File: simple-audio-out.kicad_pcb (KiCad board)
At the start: 2 copper layers, 49.5 x 72.4 mm, 12 parts, among them J1 Conn_01x04, Q1 2N3904

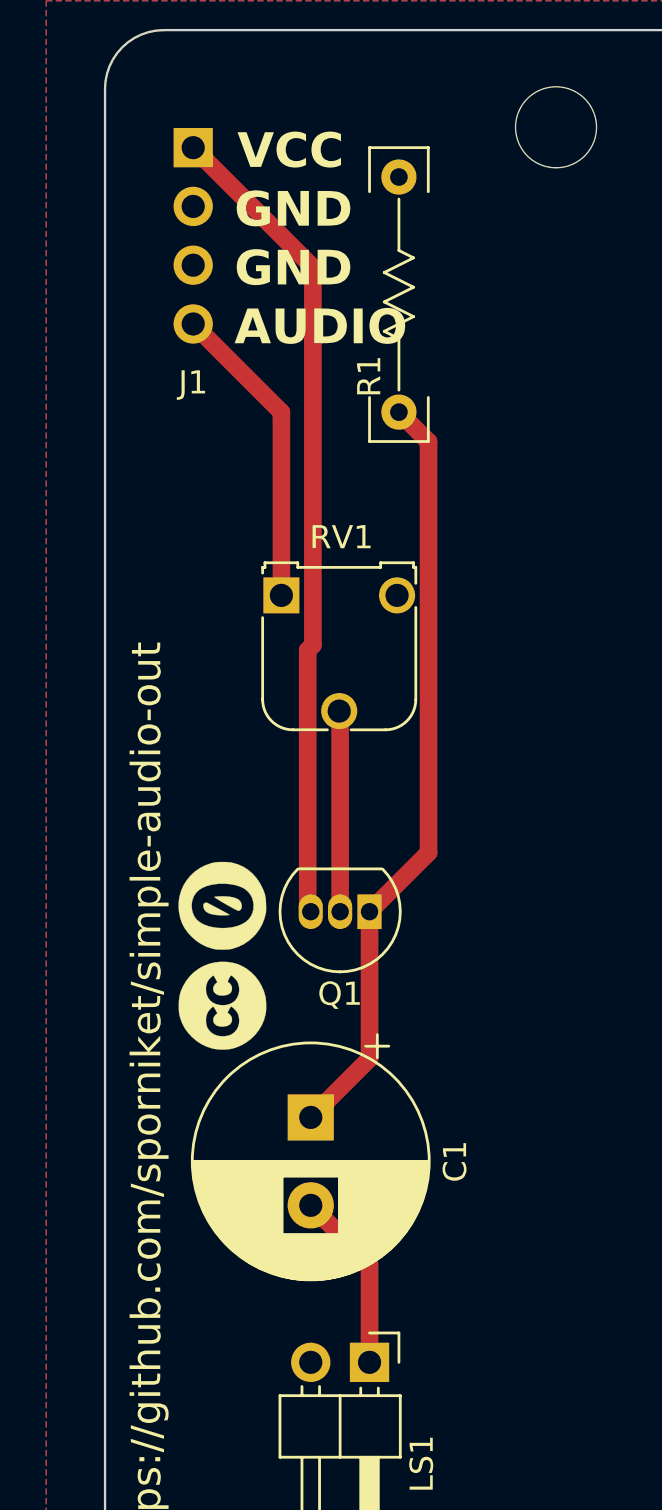
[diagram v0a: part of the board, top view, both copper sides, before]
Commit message: #1 -- change the footprint of Q1 for easier assembly
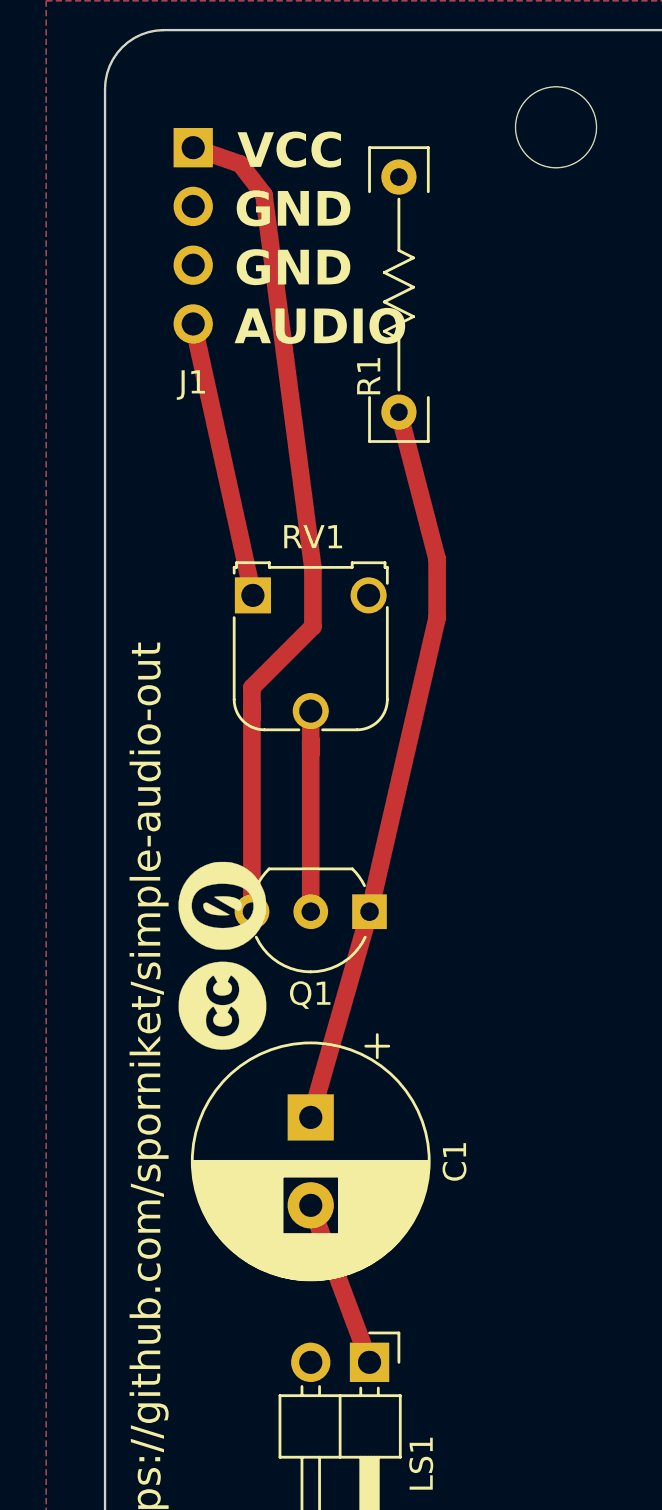
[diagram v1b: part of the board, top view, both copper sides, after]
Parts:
- Q1: footprint Package_TO_SOT_THT:TO-92_Inline -> Package_TO_SOT_THT:TO-92_Inline_Wide
- moved RV1 1.23 mm to (118.2, 43.5)
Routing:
- net Net-(Q1-E): track 33.1 -> 31.4 mm
- net /AUDIO_IN: track 13.3 -> 12.0 mm
- net /VCC: track 35.3 -> 36.5 mm
- net Net-(Q1-B): track 8.69 -> 9.44 mm
- net Net-(C1-Pad2): track 7.84 -> 7.24 mm
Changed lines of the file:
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@@
   (net 5 "/AUDIO_IN")
   (net 6 "Net-(Q1-B)")
-  (footprint "Package_TO_SOT_THT:TO-92_Inline" (layer "F.Cu")
+  (footprint "Package_TO_SOT_THT:TO-92_Inline_Wide" (layer "F.Cu")
     (at 123.19 57.15 180)
-    (descr "TO-92 leads in-line, narrow, oval pads, drill 0.75mm (see NXP sot054_po.pdf)")
+    (descr "TO-92 leads in-line, wide, drill 0.75mm (see NXP sot054_po.pdf)")
     (tags "to-92 sc-43 sc-43a sot54 PA33 transistor")
     (property "Sheetfile" "simple-audio-out.kicad_sch")
@@
     (property "ki_keywords" "NPN Transistor")
     (attr through_hole)
-    (fp_text reference "Q1" (at 1.27 -3.56) (layer "F.SilkS")
-        (effects (font (size 1 1) (thickness 0.15)))
-    )
-    (fp_text value "2N3904" (at 1.27 2.79) (layer "F.Fab")
-        (effects (font (size 1 1) (thickness 0.15)))
-    )
-    (fp_text user "${REFERENCE}" (at 1.27 0) (layer "F.Fab")
-        (effects (font (size 1 1) (thickness 0.15)))
-    )
-    (fp_line (start -0.53 1.85) (end 3.07 1.85)
-      (stroke (width 0.12) (type solid)) (layer "F.SilkS"))
-    (fp_arc (start -0.568478 1.838478) (mid -1.132087 -0.994977) (end 1.27 -2.6)
-      (stroke (width 0.12) (type solid)) (layer "F.SilkS"))
-    (fp_arc (start 1.27 -2.6) (mid 3.672087 -0.994977) (end 3.108478 1.838478)
-      (stroke (width 0.12) (type solid)) (layer "F.SilkS"))
-    (fp_line (start -1.46 -2.73) (end -1.46 2.01)
+    (fp_text reference "Q1" (at 2.54 -3.56 180) (layer "F.SilkS")
+        (effects (font (size 1 1) (thickness 0.15)))
+    )
+    (fp_text value "2N3904" (at 2.54 2.79 180) (layer "F.Fab")
+        (effects (font (size 1 1) (thickness 0.15)))
+    )
+    (fp_text user "${REFERENCE}" (at 2.54 0 180) (layer "F.Fab")
+        (effects (font (size 1 1) (thickness 0.15)))
+    )
+    (fp_line (start 0.74 1.85) (end 4.34 1.85)
+      (stroke (width 0.12) (type solid)) (layer "F.SilkS"))
+    (fp_arc (start 0.1836 -1.098807) (mid 1.143021 -2.192817) (end 2.54 -2.6)
+      (stroke (width 0.12) (type solid)) (layer "F.SilkS"))
+    (fp_arc (start 0.74 1.85) (mid 0.446097 1.509328) (end 0.215816 1.122795)
+      (stroke (width 0.12) (type solid)) (layer "F.SilkS"))
+    (fp_arc (start 2.54 -2.6) (mid 3.936979 -2.192818) (end 4.8964 -1.098807)
+      (stroke (width 0.12) (type solid)) (layer "F.SilkS"))
+    (fp_arc (start 4.864184 1.122795) (mid 4.633903 1.509328) (end 4.34 1.85)
+      (stroke (width 0.12) (type solid)) (layer "F.SilkS"))
+    (fp_line (start -1.01 -2.73) (end -1.01 2.01)
       (stroke (width 0.05) (type solid)) (layer "F.CrtYd"))
-    (fp_line (start -1.46 -2.73) (end 4 -2.73)
+    (fp_line (start -1.01 -2.73) (end 6.09 -2.73)
       (stroke (width 0.05) (type solid)) (layer "F.CrtYd"))
-    (fp_line (start 4 2.01) (end -1.46 2.01)
+    (fp_line (start 6.09 2.01) (end -1.01 2.01)
       (stroke (width 0.05) (type solid)) (layer "F.CrtYd"))
-    (fp_line (start 4 2.01) (end 4 -2.73)
+    (fp_line (start 6.09 2.01) (end 6.09 -2.73)
       (stroke (width 0.05) (type solid)) (layer "F.CrtYd"))
-    (fp_line (start -0.5 1.75) (end 3 1.75)
-      (stroke (width 0.1) (type solid)) (layer "F.Fab"))
-    (fp_arc (start -0.483625 1.753625) (mid -1.021221 -0.949055) (end 1.27 -2.48)
-      (stroke (width 0.1) (type solid)) (layer "F.Fab"))
-    (fp_arc (start 1.27 -2.48) (mid 3.561221 -0.949055) (end 3.023625 1.753625)
-      (stroke (width 0.1) (type solid)) (layer "F.Fab"))
-    (pad "1" thru_hole rect (at 0 0 180) (size 1.05 1.5) (drill 0.75) (layers "*.Cu" "*.Mask")
+    (fp_line (start 0.8 1.75) (end 4.3 1.75)
+      (stroke (width 0.1) (type solid)) (layer "F.Fab"))
+    (fp_arc (start 0.786375 1.753625) (mid 0.248779 -0.949055) (end 2.54 -2.48)
+      (stroke (width 0.1) (type solid)) (layer "F.Fab"))
+    (fp_arc (start 2.54 -2.48) (mid 4.831221 -0.949055) (end 4.293625 1.753625)
+      (stroke (width 0.1) (type solid)) (layer "F.Fab"))
+    (pad "1" thru_hole rect (at 0 0 180) (size 1.5 1.5) (drill 0.8) (layers "*.Cu" "*.Mask")
       (net 1 "Net-(Q1-E)") (pinfunction "E") (pintype "passive"))
-    (pad "2" thru_hole oval (at 1.27 0 180) (size 1.05 1.5) (drill 0.75) (layers "*.Cu" "*.Mask")
+    (pad "2" thru_hole circle (at 2.54 0 180) (size 1.5 1.5) (drill 0.8) (layers "*.Cu" "*.Mask")
       (net 6 "Net-(Q1-B)") (pinfunction "B") (pintype "passive"))
-    (pad "3" thru_hole oval (at 2.54 0 180) (size 1.05 1.5) (drill 0.75) (layers "*.Cu" "*.Mask")
+    (pad "3" thru_hole circle (at 5.08 0 180) (size 1.5 1.5) (drill 0.8) (layers "*.Cu" "*.Mask")
       (net 3 "/VCC") (pinfunction "C") (pintype "passive"))
-    (model "${KICAD6_3DMODEL_DIR}/Package_TO_SOT_THT.3dshapes/TO-92_Inline.wrl"
+    (model "${KICAD6_3DMODEL_DIR}/Package_TO_SOT_THT.3dshapes/TO-92_Inline_Wide.wrl"
       (offset (xyz 0 0 0))
       (scale (xyz 1 1 1))
@@
   )
   (footprint "Potentiometer_THT:Potentiometer_Runtron_RM-065_Vertical" (layer "F.Cu")
-    (at 119.38 43.48)
+    (at 118.15 43.48)
     (descr "Potentiometer, vertical, Trimmer, RM-065 https://components101.com/sites/default/files/component_datasheet/Preset%20Potentiometer%20%28Trimpot%29.pdf")
     (tags "Potentiometer Trimmer RM-065")
@@
     (effects (font (size 2 2) (thickness 0.15)) (justify left bottom))
   )
-  (segment (start 125.741 36.841) (end 125.741 54.599) (width 0.762) (layer "F.Cu") (net 1))
-  (segment (start 125.741 54.599) (end 123.19 57.15) (width 0.762) (layer "F.Cu") (net 1))
-  (segment (start 124.46 35.56) (end 125.741 36.841) (width 0.762) (layer "F.Cu") (net 1))
-  (segment (start 123.19 57.15) (end 123.19 63.5) (width 0.762) (layer "F.Cu") (net 1))
-  (segment (start 123.19 63.5) (end 120.65 66.04) (width 0.762) (layer "F.Cu") (net 1))
-  (segment (start 123.19 72.38) (end 120.65 69.84) (width 0.762) (layer "F.Cu") (net 2))
-  (segment (start 123.19 76.625) (end 123.19 72.38) (width 0.762) (layer "F.Cu") (net 2))
-  (segment (start 120.741 45.629) (end 120.741 29.301) (width 0.762) (layer "F.Cu") (net 3))
-  (segment (start 120.519 57.019) (end 120.519 45.851) (width 0.762) (layer "F.Cu") (net 3))
-  (segment (start 120.741 29.301) (end 115.57 24.13) (width 0.762) (layer "F.Cu") (net 3))
-  (segment (start 120.65 57.15) (end 120.519 57.019) (width 0.762) (layer "F.Cu") (net 3))
-  (segment (start 120.519 45.851) (end 120.741 45.629) (width 0.762) (layer "F.Cu") (net 3))
-  (segment (start 119.38 35.56) (end 115.57 31.75) (width 0.762) (layer "F.Cu") (net 5))
-  (segment (start 119.38 43.48) (end 119.38 35.56) (width 0.762) (layer "F.Cu") (net 5))
-  (segment (start 121.92 48.52) (end 121.88 48.48) (width 0.762) (layer "F.Cu") (net 6))
-  (segment (start 121.92 57.15) (end 121.92 48.52) (width 0.762) (layer "F.Cu") (net 6))
+  (segment (start 124.46 35.56) (end 126.111 41.91) (width 0.762) (layer "F.Cu") (net 1))
+  (segment (start 123.19 57.15) (end 126.111 44.45) (width 0.762) (layer "F.Cu") (net 1))
+  (segment (start 126.111 44.45) (end 126.111 41.91) (width 0.762) (layer "F.Cu") (net 1))
+  (segment (start 120.65 66.04) (end 123.19 57.15) (width 0.762) (layer "F.Cu") (net 1))
+  (segment (start 123.19 76.625) (end 120.65 69.84) (width 0.762) (layer "F.Cu") (net 2))
+  (segment (start 118.11 47.462) (end 118.11 48.768) (width 0.762) (layer "F.Cu") (net 3))
+  (segment (start 118.11 48.768) (end 118.11 57.15) (width 0.762) (layer "F.Cu") (net 3))
+  (segment (start 120.741 42.291) (end 118.624333 26.162) (width 0.762) (layer "F.Cu") (net 3))
+  (segment (start 120.741 44.831) (end 118.11 47.462) (width 0.762) (layer "F.Cu") (net 3))
+  (segment (start 118.11 48.26) (end 118.11 48.768) (width 0.762) (layer "F.Cu") (net 3))
+  (segment (start 115.57 24.13) (end 117.602 24.836783) (width 0.762) (layer "F.Cu") (net 3))
+  (segment (start 120.741 42.291) (end 120.741 44.831) (width 0.762) (layer "F.Cu") (net 3))
+  (segment (start 118.624333 26.162) (end 117.602 24.836783) (width 0.762) (layer "F.Cu") (net 3))
+  (segment (start 118.15 43.48) (end 115.57 31.75) (width 0.762) (layer "F.Cu") (net 5))
+  (segment (start 120.65 50.292) (end 120.65 49.71) (width 0.762) (layer "F.Cu") (net 6))
+  (segment (start 120.65 57.15) (end 120.65 50.292) (width 0.762) (layer "F.Cu") (net 6))
+  (segment (start 120.65 48.48) (end 120.65 50.292) (width 0.762) (layer "F.Cu") (net 6))
+  (segment (start 120.65 57.15) (end 120.519 57.019) (width 0.762) (layer "F.Cu") (net 6))
   (zone (net 4) (net_name "/GND") (layers "F&B.Cu") (hatch edge 0.5)
     (connect_pads (clearance 0.5))

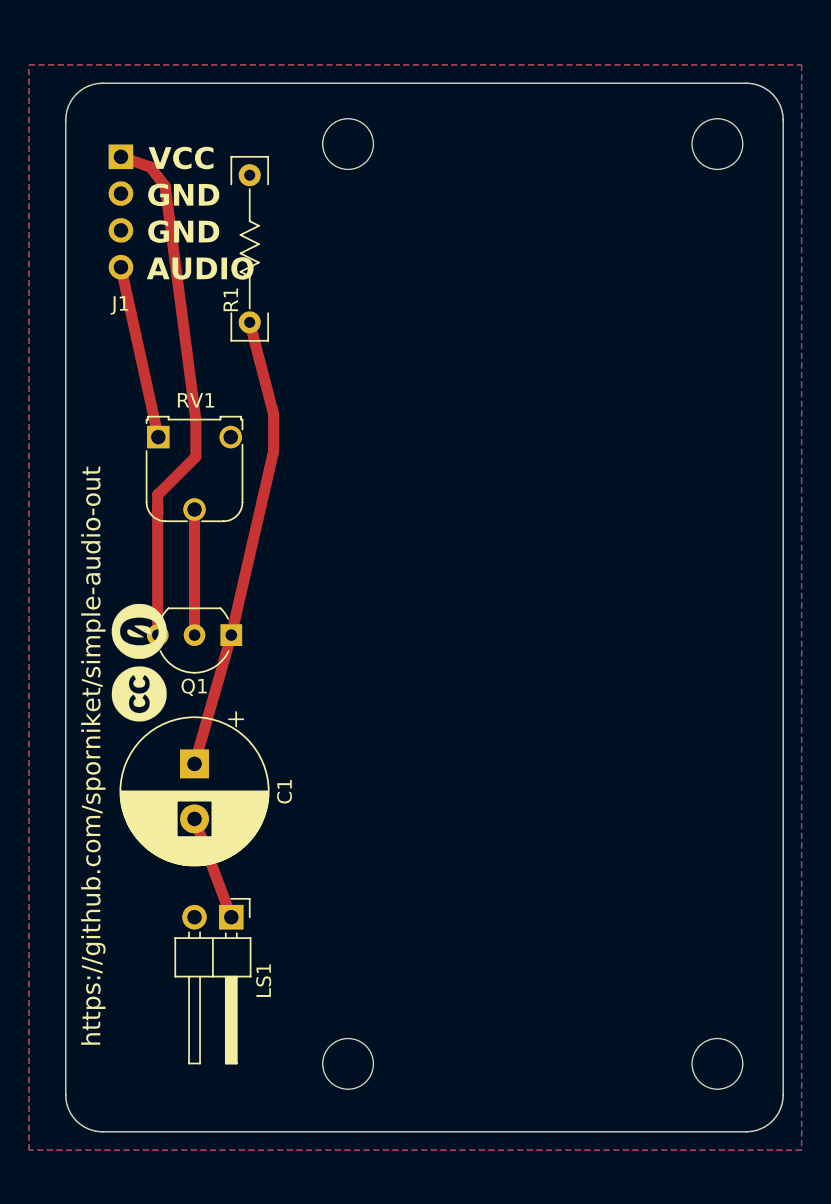
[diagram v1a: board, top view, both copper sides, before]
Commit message: #1 -- adjust the mounting holes for the speaker
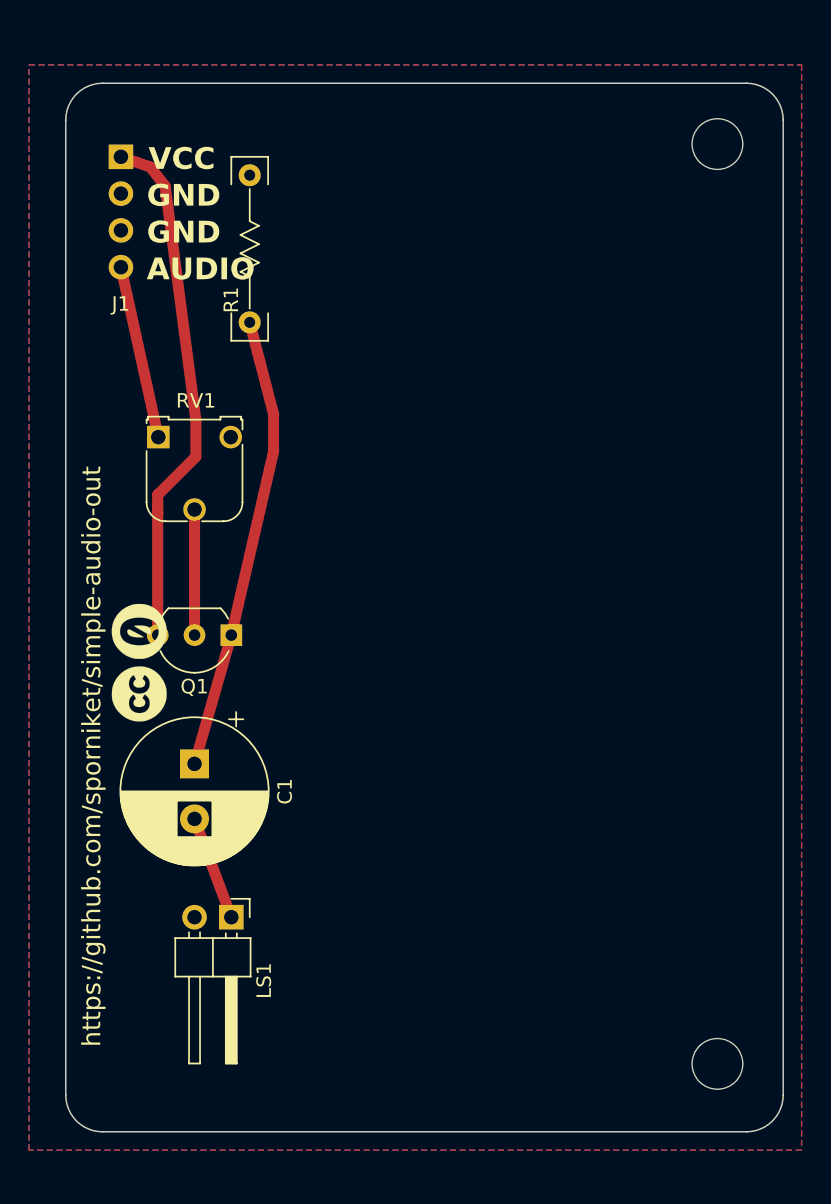
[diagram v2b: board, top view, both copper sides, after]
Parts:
- H1, H3: footprint MountingHole:MountingHole_3.5mm -> holes:MountingHole_3.5mm_room_1.5mm
- moved H1 0.75 mm to (132.0, 23.2)
- moved H3 0.75 mm to (132.0, 86.8)
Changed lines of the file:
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@@
       (stroke (width 0.01) (type solid)) (fill solid) (layer "F.SilkS"))
   )
-  (footprint "MountingHole:MountingHole_3.5mm" (layer "F.Cu")
-    (at 131.25 23.25)
-    (descr "Mounting Hole 3.5mm, no annular")
-    (tags "mounting hole 3.5mm no annular")
+  (footprint "holes:MountingHole_3.5mm_room_1.5mm" (layer "F.Cu")
+    (at 132 23.25)
+    (descr "Mounting Hole 3.5mm, no annular, with a room of 1.5mm for adjsutment.")
+    (tags "mounting hole 3.5mm no annular room 1.5mm")
     (property "Sheetfile" "simple-audio-out.kicad_sch")
     (property "Sheetname" "")
@@
         (effects (font (size 1 1) (thickness 0.15)))
     )
-    (fp_circle (center 0 0) (end 3.5 0)
-      (stroke (width 0.15) (type solid)) (fill none) (layer "Cmts.User"))
-    (fp_circle (center 0 0) (end 3.75 0)
-      (stroke (width 0.05) (type solid)) (fill none) (layer "F.CrtYd"))
-    (pad "" np_thru_hole circle (at 0 0) (size 3.5 3.5) (drill 3.5) (layers "*.Cu" "*.Mask"))
+    (fp_line (start -0.8 3.5) (end 0.8 3.5)
+      (stroke (width 0.12) (type default)) (layer "Cmts.User"))
+    (fp_line (start 0.8 -3.5) (end -0.8 -3.5)
+      (stroke (width 0.12) (type default)) (layer "Cmts.User"))
+    (fp_arc (start -0.8 3.5) (mid -4.3 0) (end -0.8 -3.5)
+      (stroke (width 0.12) (type default)) (layer "Cmts.User"))
+    (fp_arc (start 0.8 -3.5) (mid 4.3 0) (end 0.8 3.5)
+      (stroke (width 0.12) (type default)) (layer "Cmts.User"))
+    (fp_line (start -0.8 3.8) (end 0.8 3.8)
+      (stroke (width 0.05) (type default)) (layer "F.CrtYd"))
+    (fp_line (start 0.8 -3.8) (end -0.8 -3.8)
+      (stroke (width 0.05) (type default)) (layer "F.CrtYd"))
+    (fp_arc (start -0.8 3.8) (mid -4.6 0) (end -0.8 -3.8)
+      (stroke (width 0.05) (type default)) (layer "F.CrtYd"))
+    (fp_arc (start 0.8 -3.8) (mid 4.6 0) (end 0.8 3.8)
+      (stroke (width 0.05) (type default)) (layer "F.CrtYd"))
+    (pad "" np_thru_hole oval (at 0 0) (size 5 3.5) (drill oval 5 3.5) (layers "F&B.Cu" "*.Mask"))
   )
   (footprint "cliparts:logo--cc--zero" (layer "F.Cu")
@@
     (pad "" np_thru_hole circle (at 0 0) (size 3.5 3.5) (drill 3.5) (layers "*.Cu" "*.Mask"))
   )
-  (footprint "MountingHole:MountingHole_3.5mm" (layer "F.Cu")
-    (at 131.25 86.75)
-    (descr "Mounting Hole 3.5mm, no annular")
-    (tags "mounting hole 3.5mm no annular")
+  (footprint "holes:MountingHole_3.5mm_room_1.5mm" (layer "F.Cu")
+    (at 132 86.75)
+    (descr "Mounting Hole 3.5mm, no annular, with a room of 1.5mm for adjsutment.")
+    (tags "mounting hole 3.5mm no annular room 1.5mm")
     (property "Sheetfile" "simple-audio-out.kicad_sch")
     (property "Sheetname" "")
@@
         (effects (font (size 1 1) (thickness 0.15)))
     )
-    (fp_circle (center 0 0) (end 3.5 0)
-      (stroke (width 0.15) (type solid)) (fill none) (layer "Cmts.User"))
-    (fp_circle (center 0 0) (end 3.75 0)
-      (stroke (width 0.05) (type solid)) (fill none) (layer "F.CrtYd"))
-    (pad "" np_thru_hole circle (at 0 0) (size 3.5 3.5) (drill 3.5) (layers "*.Cu" "*.Mask"))
+    (fp_line (start -0.8 3.5) (end 0.8 3.5)
+      (stroke (width 0.12) (type default)) (layer "Cmts.User"))
+    (fp_line (start 0.8 -3.5) (end -0.8 -3.5)
+      (stroke (width 0.12) (type default)) (layer "Cmts.User"))
+    (fp_arc (start -0.8 3.5) (mid -4.3 0) (end -0.8 -3.5)
+      (stroke (width 0.12) (type default)) (layer "Cmts.User"))
+    (fp_arc (start 0.8 -3.5) (mid 4.3 0) (end 0.8 3.5)
+      (stroke (width 0.12) (type default)) (layer "Cmts.User"))
+    (fp_line (start -0.8 3.8) (end 0.8 3.8)
+      (stroke (width 0.05) (type default)) (layer "F.CrtYd"))
+    (fp_line (start 0.8 -3.8) (end -0.8 -3.8)
+      (stroke (width 0.05) (type default)) (layer "F.CrtYd"))
+    (fp_arc (start -0.8 3.8) (mid -4.6 0) (end -0.8 -3.8)
+      (stroke (width 0.05) (type default)) (layer "F.CrtYd"))
+    (fp_arc (start 0.8 -3.8) (mid 4.6 0) (end 0.8 3.8)
+      (stroke (width 0.05) (type default)) (layer "F.CrtYd"))
+    (pad "" np_thru_hole oval (at 0 0) (size 5 3.5) (drill oval 5 3.5) (layers "F&B.Cu" "*.Mask"))
   )
   (footprint "Potentiometer_THT:Potentiometer_Runtron_RM-065_Vertical" (layer "F.Cu")
